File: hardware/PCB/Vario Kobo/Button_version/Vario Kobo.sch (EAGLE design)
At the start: 24 parts

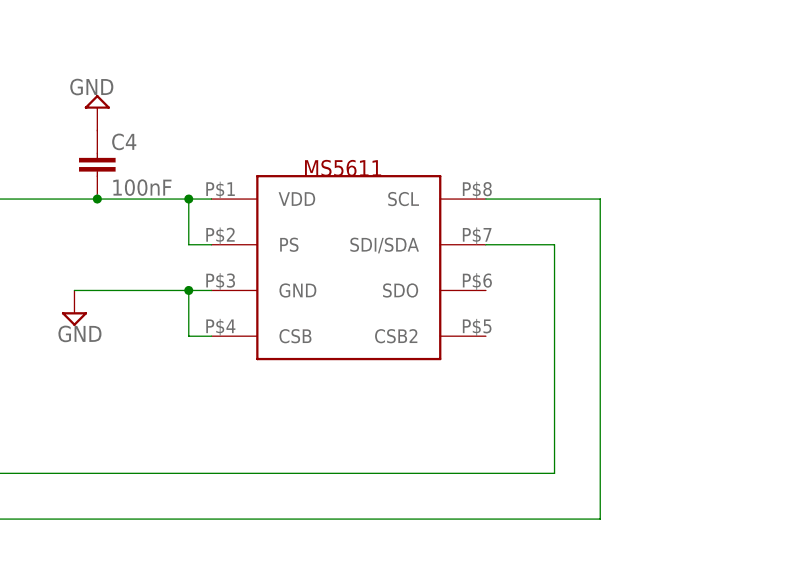
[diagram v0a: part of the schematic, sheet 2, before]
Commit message: CLEAN
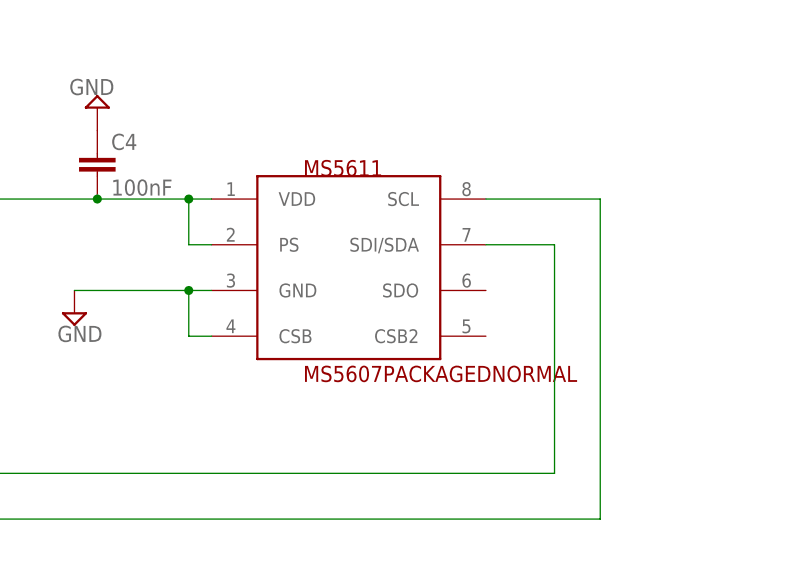
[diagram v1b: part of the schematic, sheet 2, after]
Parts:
- MS5611: value MS5607PACKAGED -> MS5607PACKAGEDNORMAL; device measurement_specialties:MS5607PACKAGED -> measurement_specialties:MS5607PACKAGEDNORMAL
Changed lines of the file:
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@@
 <?xml version="1.0" encoding="utf-8"?>
 <!DOCTYPE eagle SYSTEM "eagle.dtd">
-<eagle version="6.1">
+<eagle version="7.3.0">
 <drawing>
 <settings>
@@
 <layer number="48" name="Document" color="7" fill="1" visible="no" active="no"/>
 <layer number="49" name="Reference" color="7" fill="1" visible="no" active="no"/>
+<layer number="50" name="dxf" color="7" fill="1" visible="no" active="no"/>
 <layer number="51" name="tDocu" color="7" fill="1" visible="no" active="no"/>
 <layer number="52" name="bDocu" color="7" fill="1" visible="no" active="no"/>
+<layer number="53" name="tGND_GNDA" color="7" fill="9" visible="no" active="no"/>
+<layer number="54" name="bGND_GNDA" color="1" fill="9" visible="no" active="no"/>
+<layer number="56" name="wert" color="7" fill="1" visible="no" active="no"/>
+<layer number="57" name="tCAD" color="7" fill="1" visible="no" active="no"/>
+<layer number="59" name="tCarbon" color="7" fill="1" visible="no" active="no"/>
+<layer number="60" name="bCarbon" color="7" fill="1" visible="no" active="no"/>
+<layer number="90" name="Modules" color="7" fill="1" visible="no" active="no"/>
 <layer number="91" name="Nets" color="2" fill="1" visible="yes" active="yes"/>
 <layer number="92" name="Busses" color="1" fill="1" visible="yes" active="yes"/>
@@
 <layer number="97" name="Info" color="7" fill="1" visible="yes" active="yes"/>
 <layer number="98" name="Guide" color="6" fill="1" visible="yes" active="yes"/>
+<layer number="99" name="SpiceOrder" color="7" fill="1" visible="no" active="no"/>
+<layer number="100" name="Muster" color="7" fill="1" visible="no" active="no"/>
+<layer number="101" name="Patch_Top" color="12" fill="4" visible="yes" active="yes"/>
+<layer number="102" name="Vscore" color="7" fill="1" visible="yes" active="yes"/>
+<layer number="103" name="fp3" color="7" fill="1" visible="yes" active="yes"/>
+<layer number="104" name="Name" color="7" fill="1" visible="yes" active="yes"/>
+<layer number="105" name="Beschreib" color="9" fill="1" visible="yes" active="yes"/>
+<layer number="106" name="BGA-Top" color="4" fill="1" visible="yes" active="yes"/>
+<layer number="107" name="BD-Top" color="5" fill="1" visible="yes" active="yes"/>
+<layer number="108" name="fp8" color="7" fill="1" visible="yes" active="yes"/>
+<layer number="109" name="fp9" color="7" fill="1" visible="yes" active="yes"/>
+<layer number="110" name="fp0" color="7" fill="1" visible="yes" active="yes"/>
+<layer number="111" name="LPC17xx" color="7" fill="1" visible="yes" active="yes"/>
+<layer number="112" name="tSilk" color="7" fill="1" visible="yes" active="yes"/>
+<layer number="113" name="ReferenceLS" color="7" fill="1" visible="no" active="no"/>
+<layer number="116" name="Patch_BOT" color="9" fill="4" visible="yes" active="yes"/>
+<layer number="118" name="Rect_Pads" color="7" fill="1" visible="no" active="no"/>
+<layer number="121" name="_tsilk" color="7" fill="1" visible="yes" active="yes"/>
+<layer number="122" name="_bsilk" color="7" fill="1" visible="yes" active="yes"/>
+<layer number="123" name="tTestmark" color="7" fill="1" visible="yes" active="yes"/>
+<layer number="124" name="bTestmark" color="7" fill="1" visible="yes" active="yes"/>
+<layer number="125" name="_tNames" color="7" fill="1" visible="yes" active="yes"/>
+<layer number="126" name="_bNames" color="7" fill="1" visible="yes" active="yes"/>
+<layer number="127" name="_tValues" color="7" fill="1" visible="yes" active="yes"/>
+<layer number="128" name="_bValues" color="7" fill="1" visible="yes" active="yes"/>
+<layer number="129" name="Mask" color="7" fill="1" visible="yes" active="yes"/>
+<layer number="131" name="tAdjust" color="7" fill="1" visible="yes" active="yes"/>
+<layer number="132" name="bAdjust" color="7" fill="1" visible="yes" active="yes"/>
+<layer number="144" name="Drill_legend" color="7" fill="1" visible="yes" active="yes"/>
+<layer number="150" name="Notes" color="7" fill="1" visible="yes" active="yes"/>
+<layer number="151" name="HeatSink" color="7" fill="1" visible="yes" active="yes"/>
+<layer number="152" name="_bDocu" color="7" fill="1" visible="yes" active="yes"/>
+<layer number="153" name="FabDoc1" color="6" fill="1" visible="no" active="no"/>
+<layer number="154" name="FabDoc2" color="2" fill="1" visible="no" active="no"/>
+<layer number="155" name="FabDoc3" color="7" fill="15" visible="no" active="no"/>
+<layer number="199" name="Contour" color="7" fill="1" visible="yes" active="yes"/>
+<layer number="200" name="200bmp" color="1" fill="10" visible="yes" active="yes"/>
+<layer number="201" name="201bmp" color="2" fill="1" visible="no" active="no"/>
+<layer number="202" name="202bmp" color="3" fill="1" visible="no" active="no"/>
+<layer number="203" name="203bmp" color="4" fill="10" visible="yes" active="yes"/>
+<layer number="204" name="204bmp" color="5" fill="10" visible="yes" active="yes"/>
+<layer number="205" name="205bmp" color="6" fill="10" visible="yes" active="yes"/>
+<layer number="206" name="206bmp" color="7" fill="10" visible="yes" active="yes"/>
+<layer number="207" name="207bmp" color="8" fill="10" visible="yes" active="yes"/>
+<layer number="208" name="208bmp" color="9" fill="10" visible="yes" active="yes"/>
+<layer number="209" name="209bmp" color="7" fill="1" visible="yes" active="yes"/>
+<layer number="210" name="210bmp" color="7" fill="1" visible="yes" active="yes"/>
+<layer number="211" name="211bmp" color="7" fill="1" visible="yes" active="yes"/>
+<layer number="212" name="212bmp" color="7" fill="1" visible="yes" active="yes"/>
+<layer number="213" name="213bmp" color="7" fill="1" visible="yes" active="yes"/>
+<layer number="214" name="214bmp" color="7" fill="1" visible="yes" active="yes"/>
+<layer number="215" name="215bmp" color="7" fill="1" visible="yes" active="yes"/>
+<layer number="216" name="216bmp" color="7" fill="1" visible="yes" active="yes"/>
+<layer number="217" name="217bmp" color="18" fill="1" visible="no" active="no"/>
+<layer number="218" name="218bmp" color="19" fill="1" visible="no" active="no"/>
+<layer number="219" name="219bmp" color="20" fill="1" visible="no" active="no"/>
+<layer number="220" name="220bmp" color="21" fill="1" visible="no" active="no"/>
+<layer number="221" name="221bmp" color="22" fill="1" visible="no" active="no"/>
+<layer number="222" name="222bmp" color="23" fill="1" visible="no" active="no"/>
+<layer number="223" name="223bmp" color="24" fill="1" visible="no" active="no"/>
+<layer number="224" name="224bmp" color="25" fill="1" visible="no" active="no"/>
+<layer number="225" name="225bmp" color="7" fill="1" visible="yes" active="yes"/>
+<layer number="226" name="226bmp" color="7" fill="1" visible="yes" active="yes"/>
+<layer number="227" name="227bmp" color="7" fill="1" visible="yes" active="yes"/>
+<layer number="228" name="228bmp" color="7" fill="1" visible="yes" active="yes"/>
+<layer number="229" name="229bmp" color="7" fill="1" visible="yes" active="yes"/>
+<layer number="230" name="230bmp" color="7" fill="1" visible="yes" active="yes"/>
+<layer number="231" name="Eagle3D_PG1" color="7" fill="1" visible="no" active="no"/>
+<layer number="232" name="Eagle3D_PG2" color="7" fill="1" visible="no" active="no"/>
+<layer number="233" name="Eagle3D_PG3" color="7" fill="1" visible="no" active="no"/>
+<layer number="248" name="Housing" color="7" fill="1" visible="yes" active="yes"/>
+<layer number="249" name="Edge" color="7" fill="1" visible="yes" active="yes"/>
+<layer number="250" name="Descript" color="7" fill="1" visible="no" active="no"/>
+<layer number="251" name="SMDround" color="7" fill="1" visible="no" active="no"/>
+<layer number="254" name="cooling" color="7" fill="1" visible="yes" active="yes"/>
+<layer number="255" name="routoute" color="7" fill="1" visible="yes" active="yes"/>
 </layers>
 <schematic xreflabel="%F%N/%S.%C%R" xrefpart="/%S.%C%R">
@@
 </classes>
 <parts>
-<part name="PIC" library="microchip" deviceset="PIC24F16KA101-X_" device="" value=""/>
+<part name="PIC" library="microchip" deviceset="PIC24F16KA101-X_" device="" value="PIC24F16KA101-X_"/>
 <part name="SUPPLY5" library="supply2" deviceset="GND" device=""/>
 <part name="C3" library="rcl" deviceset="C-EU" device="C0603" value="100nF"/>
 <part name="SUPPLY6" library="supply2" deviceset="GND" device=""/>
-<part name="MS5611" library="measurement_specialties" deviceset="MS5607PACKAGED" device="" value=""/>
+<part name="MS5611" library="measurement_specialties" deviceset="MS5607PACKAGED" device="NORMAL" value="MS5607PACKAGEDNORMAL"/>
 <part name="SUPPLY7" library="supply2" deviceset="GND" device=""/>
 <part name="C4" library="rcl" deviceset="C-EU" device="C0603" value="100nF"/>
